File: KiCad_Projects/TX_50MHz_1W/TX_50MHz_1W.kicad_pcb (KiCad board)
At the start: 2 copper layers, 232.3 x 186.9 mm, 51 parts, among them J1 AIL Stick, J10 I2C Exp / OLED, J11 ANT, J2 ELE Stick, J3 THR Stick, J4 RUD Stick, J5 AUX6, J6 AUX5, J7 AUX7, J8 V_BATT In (XT30), J9 5V Logic In, Q1 RD01MUS2 (1W PA), U1 ESP32-S3-WROOM-1-N16R8, U10 AP2112K-3.3TRG1, U2 Si5351A-B-GT, U3 BGS12SN6E6327XTSA1 (T/R SW), U4 SPF5043Z (LNA), U5 LT5560 (Mixer), U6 ADS1115IDGSR (0x48), U7 ADS1115IDGSR (0x49), U8 SH1106 1.3in OLED, U9 LMR33630BDDA, Y1 26.000MHz

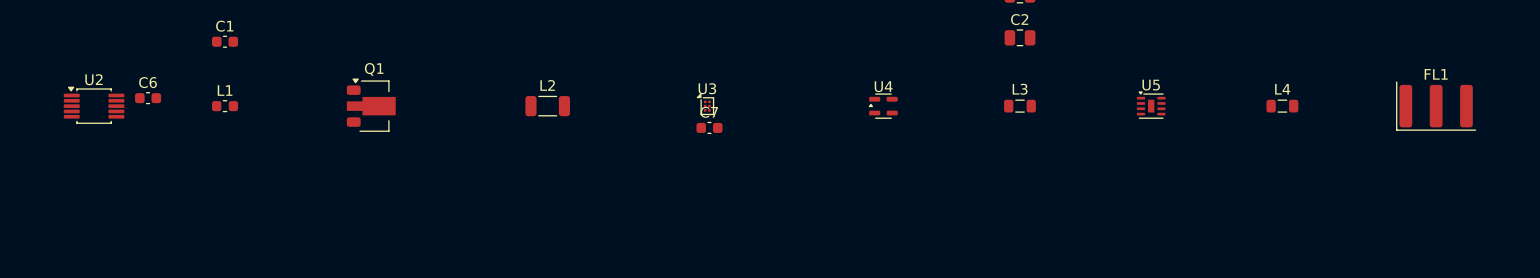
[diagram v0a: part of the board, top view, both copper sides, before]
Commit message: broke up scheamatics into multiple files for easier navigation and organization. Added a new schematic page for organizing the schematics.  Added a new schematic page for the RX controller IO.  Added a new schematic page for the RX IF radio.  Added a new schematic page for the RX RF front end.  Added a new schematic page for the TX battery power.  Added a new schematic page for the TX controller RF.  Added a new schematic page for the TX telemetry IF.
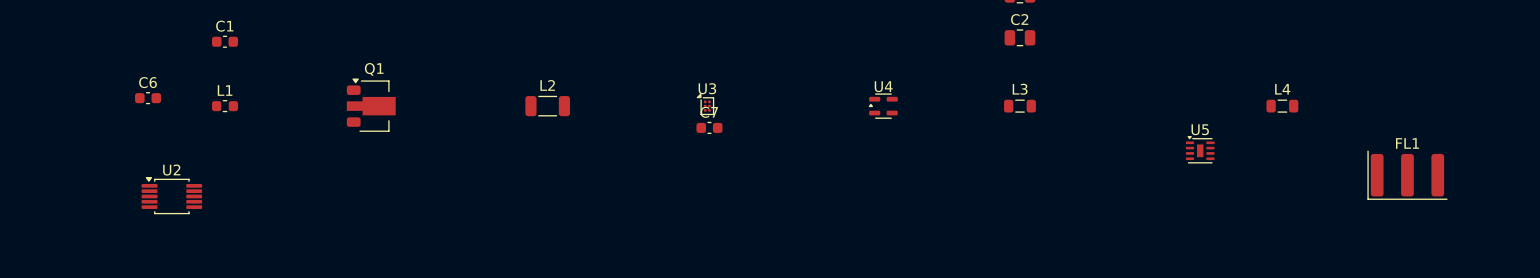
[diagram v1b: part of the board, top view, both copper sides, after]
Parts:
- moved U2 11.2 mm to (40.6, 43.5)
- moved FL1 7.04 mm to (156.8, 41.5)
- moved U5 6.24 mm to (137.3, 39.2)
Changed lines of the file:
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@@
 	(footprint "DFN-8-1EP_2x2mm_P0.5mm_EP0.6x1.2mm"
 		(layer "F.Cu")
-		(at 132.738092 35)
+		(at 137.35 39.2)
 		(descr "DFN, 8 Pin (https://www.onsemi.com/pub/Collateral/506AQ.PDF)")
 		(tags "DFN NoLead 506AQ")
@@
 		(duplicate_pad_numbers_are_jumpers no)
 		(fp_line
-			(start -3.71 -0.25)
-			(end -3.71 0.25)
+			(start -3.21 0)
+			(end -3.71 -0.25)
 			(stroke
 				(width 0.12)
@@
 		)
 		(fp_line
-			(start -3.21 0)
-			(end -3.71 -0.25)
+			(start -3.71 -0.25)
+			(end -3.71 0.25)
 			(stroke
 				(width 0.12)
@@
 		)
 		(fp_line
-			(start -3.04 5.58)
-			(end -3.04 -5.58)
+			(start 14.47 5.58)
+			(end -3.04 5.58)
 			(stroke
 				(width 0.05)
@@
 		(fp_line
 			(start 14.47 -5.58)
-			(end -3.04 -5.58)
+			(end 14.47 5.58)
 			(stroke
 				(width 0.05)
@@
 		(fp_line
 			(start 14.47 -5.58)
-			(end 14.47 5.58)
+			(end -3.04 -5.58)
 			(stroke
 				(width 0.05)
@@
 		)
 		(fp_line
-			(start 14.47 5.58)
-			(end -3.04 5.58)
+			(start -3.04 5.58)
+			(end -3.04 -5.58)
 			(stroke
 				(width 0.05)
@@
 		)
 		(fp_line
-			(start -3.04 5.58)
-			(end -3.04 -5.58)
+			(start 14.47 5.58)
+			(end -3.04 5.58)
 			(stroke
 				(width 0.05)
@@
 		(fp_line
 			(start 14.47 -5.58)
-			(end -3.04 -5.58)
+			(end 14.47 5.58)
 			(stroke
 				(width 0.05)
@@
 		(fp_line
 			(start 14.47 -5.58)
-			(end 14.47 5.58)
+			(end -3.04 -5.58)
 			(stroke
 				(width 0.05)
@@
 		)
 		(fp_line
-			(start 14.47 5.58)
-			(end -3.04 5.58)
+			(start -3.04 5.58)
+			(end -3.04 -5.58)
 			(stroke
 				(width 0.05)
@@
 		)
 		(fp_line
-			(start -1.91 -5.08)
-			(end -1.91 -3.81)
+			(start 13.97 3.81)
+			(end 4.445 3.81)
 			(stroke
 				(width 0.1)
@@
 		)
 		(fp_line
-			(start -1.91 -5.08)
-			(end 4.445 -5.08)
+			(start 13.97 -3.81)
+			(end 13.97 3.81)
 			(stroke
 				(width 0.1)
@@
 		)
 		(fp_line
-			(start -1.91 -3.81)
-			(end 2.54 -3.81)
+			(start 4.445 5.08)
+			(end 4.445 3.81)
 			(stroke
 				(width 0.1)
@@
 		)
 		(fp_line
-			(start -1.91 3.81)
-			(end -1.91 5.08)
+			(start 4.445 -3.81)
+			(end 13.97 -3.81)
 			(stroke
 				(width 0.1)
@@
 		)
 		(fp_line
-			(start -1.91 5.08)
-			(end 4.445 5.08)
+			(start 4.445 -3.81)
+			(end 4.445 -5.08)
 			(stroke
 				(width 0.1)
@@
 		)
 		(fp_line
-			(start 2.54 -3.81)
-			(end 2.54 3.81)
+			(start 3.54 0)
+			(end 2.54 0.75)
 			(stroke
 				(width 0.1)
@@
 		)
 		(fp_line
-			(start 2.54 -0.75)
-			(end 3.54 0)
+			(start 2.54 3.81)
+			(end -1.91 3.81)
 			(stroke
 				(width 0.1)
@@
 		)
 		(fp_line
-			(start 2.54 3.81)
-			(end -1.91 3.81)
+			(start 2.54 -0.75)
+			(end 3.54 0)
 			(stroke
 				(width 0.1)
@@
 		)
 		(fp_line
-			(start 3.54 0)
-			(end 2.54 0.75)
+			(start 2.54 -3.81)
+			(end 2.54 3.81)
 			(stroke
 				(width 0.1)
@@
 		)
 		(fp_line
-			(start 4.445 -3.81)
-			(end 4.445 -5.08)
+			(start -1.91 5.08)
+			(end 4.445 5.08)
 			(stroke
 				(width 0.1)
@@
 		)
 		(fp_line
-			(start 4.445 -3.81)
-			(end 13.97 -3.81)
+			(start -1.91 3.81)
+			(end -1.91 5.08)
 			(stroke
 				(width 0.1)
@@
 		)
 		(fp_line
-			(start 4.445 5.08)
-			(end 4.445 3.81)
+			(start -1.91 -3.81)
+			(end 2.54 -3.81)
 			(stroke
 				(width 0.1)
@@
 		)
 		(fp_line
-			(start 13.97 -3.81)
-			(end 13.97 3.81)
+			(start -1.91 -5.08)
+			(end 4.445 -5.08)
 			(stroke
 				(width 0.1)
@@
 		)
 		(fp_line
-			(start 13.97 3.81)
-			(end 4.445 3.81)
+			(start -1.91 -5.08)
+			(end -1.91 -3.81)
 			(stroke
 				(width 0.1)
@@
 	(footprint "MSOP-10_3x3mm_P0.5mm"
 		(layer "F.Cu")
-		(at 33.279761 35)
+		(at 40.6 43.5)
 		(descr "MSOP, 10 Pin (JEDEC MO-187 variation BA, 0.85mm body thickness, https://www.jedec.org/system/files/docs/mo-187F.pdf)")
 		(tags "MSOP SO TSSOP-10_3x3mm_P0.5mm")
@@
 	(footprint "Resonator_SMD_Murata_SFECV-3Pin_6.9x2.9mm"
 		(layer "F.Cu")
-		(at 159.547617 35)
+		(at 156.85 41.5)
 		(descr "Murata SFECV, Resonator/Filter, 6.9x2.9mm package, SMD, http://cdn-reichelt.de/documents/datenblatt/B400/SFECV-107.pdf")
 		(tags "ceramic")
